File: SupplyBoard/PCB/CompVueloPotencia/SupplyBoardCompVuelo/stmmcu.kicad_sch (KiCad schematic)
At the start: 20 parts, among them J2 USB_B_Micro, J3 ST_LINK, SW1 Reset, SW4 SW_SPDT, U3 STM32F103CBT6, Y1 16MHz

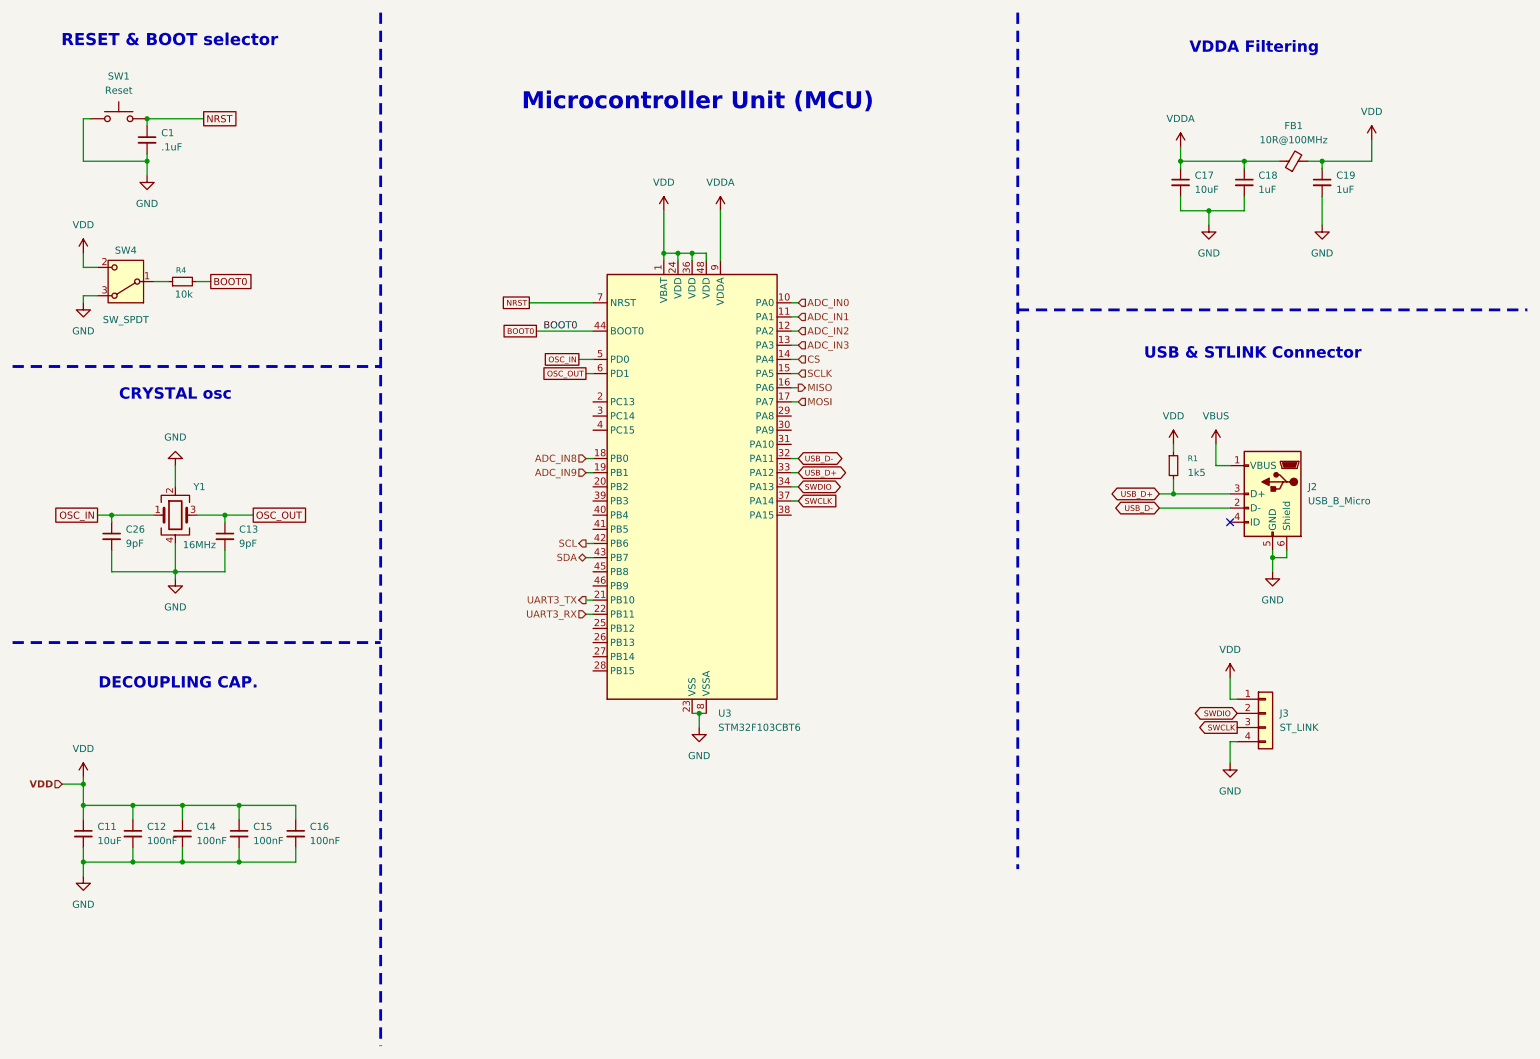
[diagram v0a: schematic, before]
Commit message: Supply Board - Remake Schematic in KiCad 9
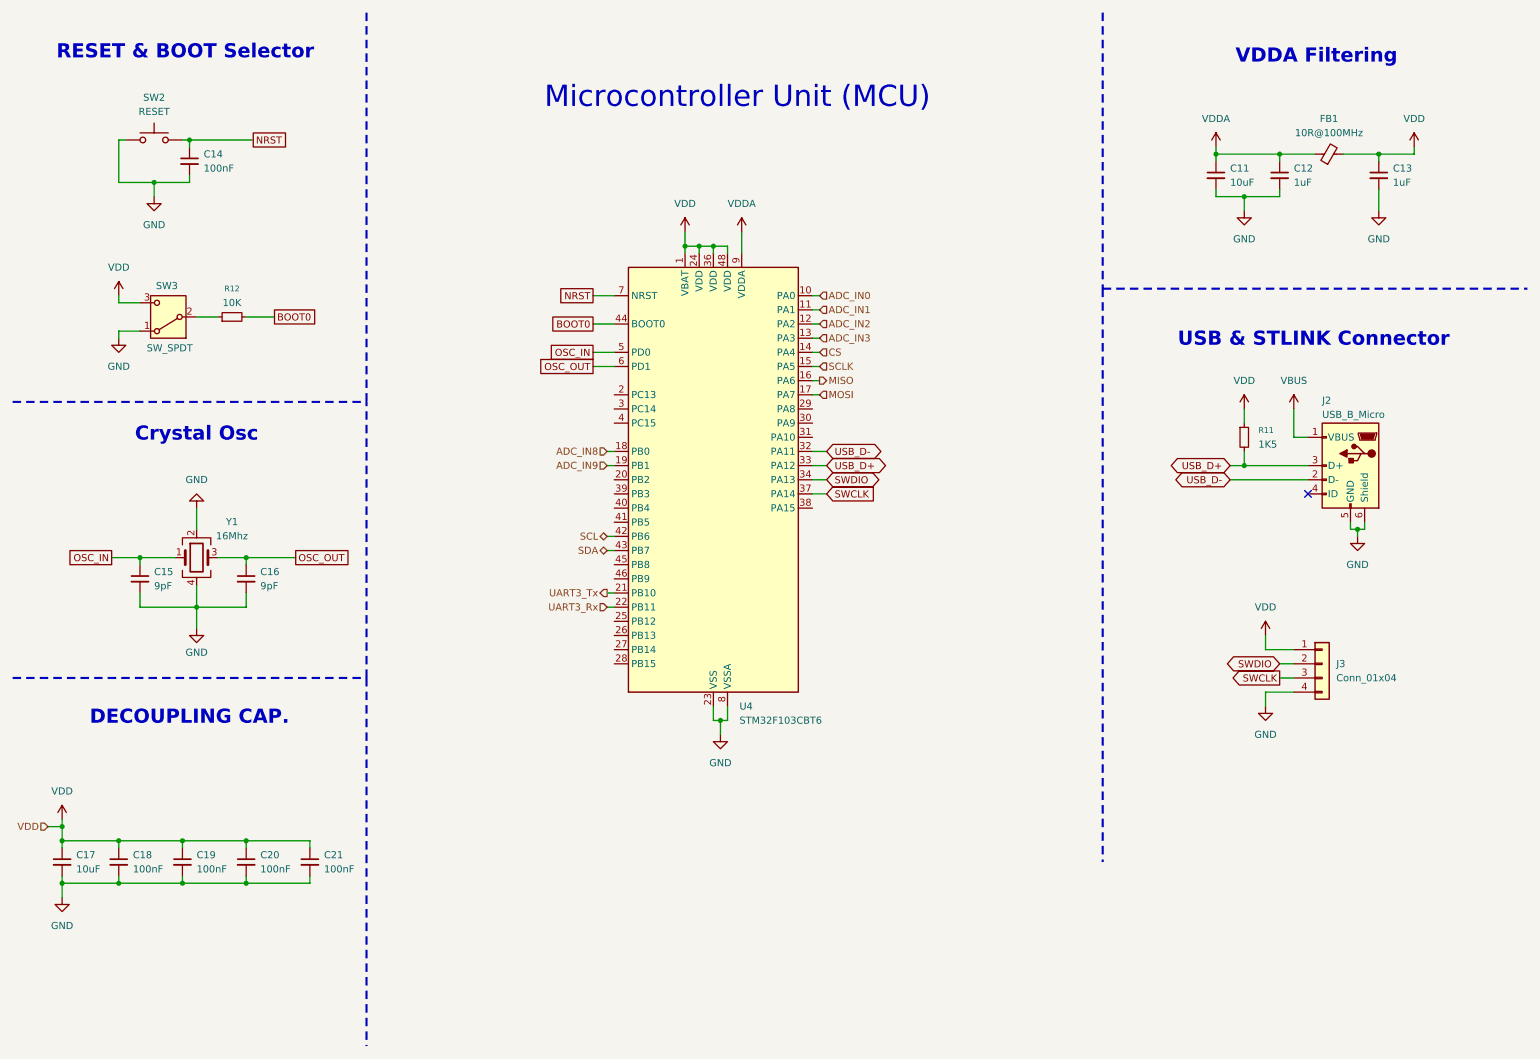
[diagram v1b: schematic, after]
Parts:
- removed C1: .1uF, Capacitor_SMD:C_0805_2012Metric, symbol Device:C_Small
- removed C26: 9pF, Resistor_SMD:R_0805_2012Metric, symbol Device:C_Small
- removed R1: 1k5, Resistor_SMD:R_0805_2012Metric, symbol Device:R_Small
- removed R4: 10k, Resistor_SMD:R_0805_2012Metric, symbol Device:R_Small
- removed SW1: Reset, Button_Switch_SMD:SW_SPST_SKQG_WithStem, symbol Switch:SW_Push
- removed SW4: SW_SPDT, SPDT_Big:SolderWire-0.5sqmm_1x03_P4.8mm_D0.9mm_OD2.3mm, symbol Switch:SW_SPDT_312
- removed U3: STM32F103CBT6, Package_QFP:LQFP-48_7x7mm_P0.5mm, symbol MCU_ST_STM32F1:STM32F103CBTx
- added C20, C21: 100nF, symbol Device:C_Small
- added R11: 1K5, symbol Device:R_Small
- added R12: 10K, symbol Device:R_Small
- added SW2: RESET, symbol Switch:SW_Push
- added SW3: SW_SPDT, symbol Switch:SW_SPDT
- added U4: STM32F103CBT6, Package_QFP:LQFP-48_7x7mm_P0.5mm, symbol MCU_ST_STM32F1:STM32F103CBTx
- C11, C14, C17: footprint Capacitor_SMD:C_0805_2012Metric -> (none)
- C12: value 100nF -> 1uF; footprint Capacitor_SMD:C_0805_2012Metric -> (none)
- C13: value 9pF -> 1uF; footprint Resistor_SMD:R_0805_2012Metric -> (none)
- C15, C16: value 100nF -> 9pF; footprint Capacitor_SMD:C_0805_2012Metric -> (none)
- C18, C19: value 1uF -> 100nF; footprint Capacitor_SMD:C_0805_2012Metric -> (none)
- FB1: footprint Inductor_SMD:L_0201_0603Metric -> (none)
- J2: footprint Connector_USB:USB_Micro-B_Amphenol_10118194_Horizontal -> (none)
- J3: value ST_LINK -> Conn_01x04; footprint Connector_PinHeader_2.54mm:PinHeader_1x04_P2.54mm_Vertical -> (none)
- Y1: value 16MHz -> 16Mhz; footprint Crystal:Crystal_SMD_3225-4Pin_3.2x2.5mm -> (none)
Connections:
- net ADC_IN0: now also U4.10 (PA0)
- net ADC_IN1: now also U4.11 (PA1)
- net ADC_IN2: now also U4.12 (PA2)
- net ADC_IN3: now also U4.13 (PA3)
- net ADC_IN8: now also U4.18 (PB0)
- net ADC_IN9: now also U4.19 (PB1)
- net BOOT0: now also R12.2, U4.44 (BOOT0)
- net CS: now also U4.14 (PA4)
- net GND: now also C20.2, C21.2, SW2.1, SW3.1 (A), U4.23 (VSS), U4.35 (VSS), U4.47 (VSS), U4.8 (VSSA)
- net MISO: now also U4.16 (PA6)
- net MOSI: now also U4.17 (PA7)
- net NRST: now also C14.1, SW2.2, U4.7 (NRST)
- net OSC_IN: now also C15.1, U4.5 (PD0)
- net OSC_OUT: now also C16.1, U4.6 (PD1); no longer C13.1
- net SCL: now also U4.42 (PB6)
- net SCLK: now also U4.15 (PA5)
- net SDA: now also U4.43 (PB7)
- net SWCLK: now also U4.37 (PA14)
- net SWDIO: now also U4.34 (PA13)
- net USB_D+: now also R11.2, U4.33 (PA12)
- net USB_D-: now also U4.32 (PA11)
- net VDD: now also C13.1, C17.1, C18.1, C20.1, C21.1, R11.1, SW3.3 (C), U4.1 (VBAT), U4.24 (VDD), U4.36 (VDD), U4.48 (VDD); no longer C11.1, C12.1, C14.1, C15.1, C16.1
- net VDDA: now also C11.1, C12.1, U4.9 (VDDA); no longer C17.1, C18.1
- new net: R12.1, SW3.2 (B)
- new net UART3_Rx: U4.22 (PB11)
- new net UART3_Tx: U4.21 (PB10)
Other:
- note added: "Crystal Osc"
- note added: "RESET & BOOT Selector"
- note removed: "CRYSTAL osc"
- note removed: "RESET & BOOT selector"
- company: XIMBAL EK ELECTRONICA -> (none)
- title: STM32F103CBT6  Integration Schematic -> (none)
